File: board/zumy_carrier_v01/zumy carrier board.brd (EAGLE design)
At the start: 54 x 88.9 mm, 20 parts, among them J1 ODROID_POWER, J2 BATT_POWER, M1 POLOLU_STEP_DOWN, M2 ITG/MPU_MODULE, M3 POLOLU_DRV8833_MODULE, SW1 500SSP1S1M6QEA

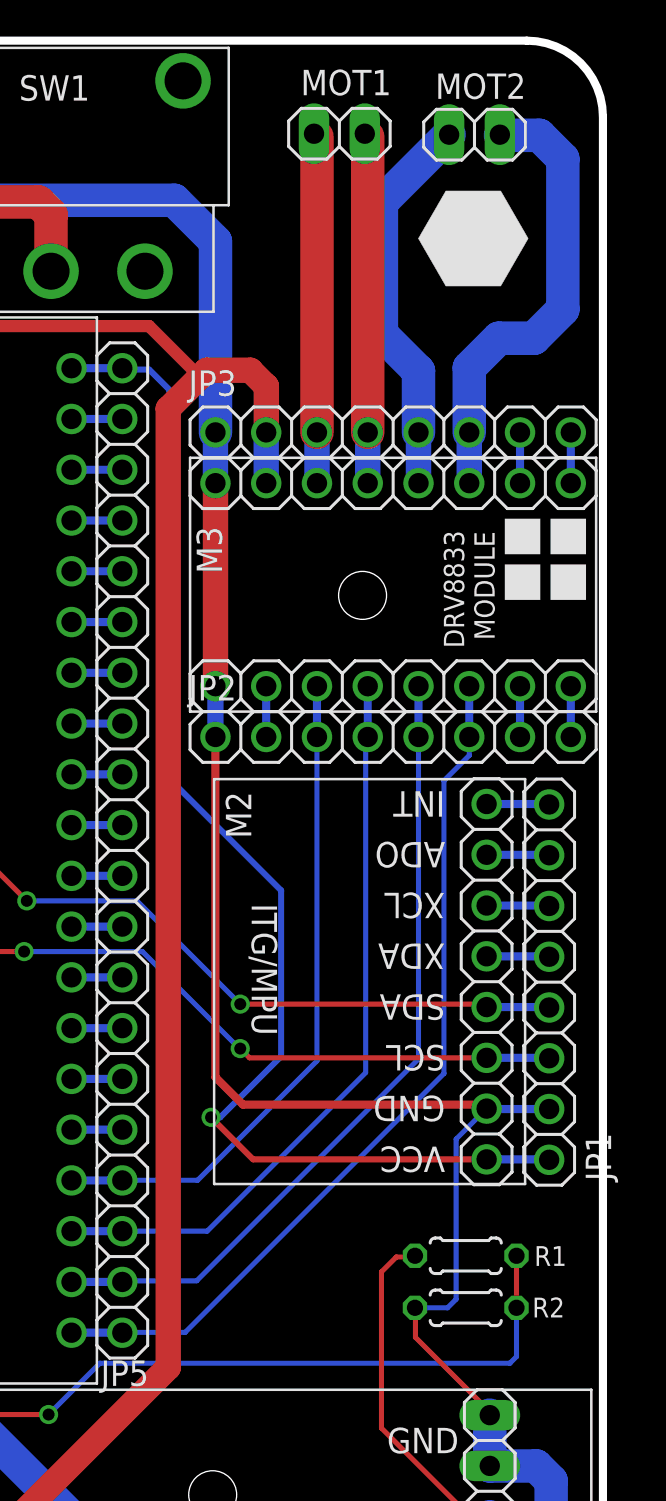
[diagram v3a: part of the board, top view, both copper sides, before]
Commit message: Added 6pin shrouded connectors for pololu encoder + motor drive. Routing is all screwed up.
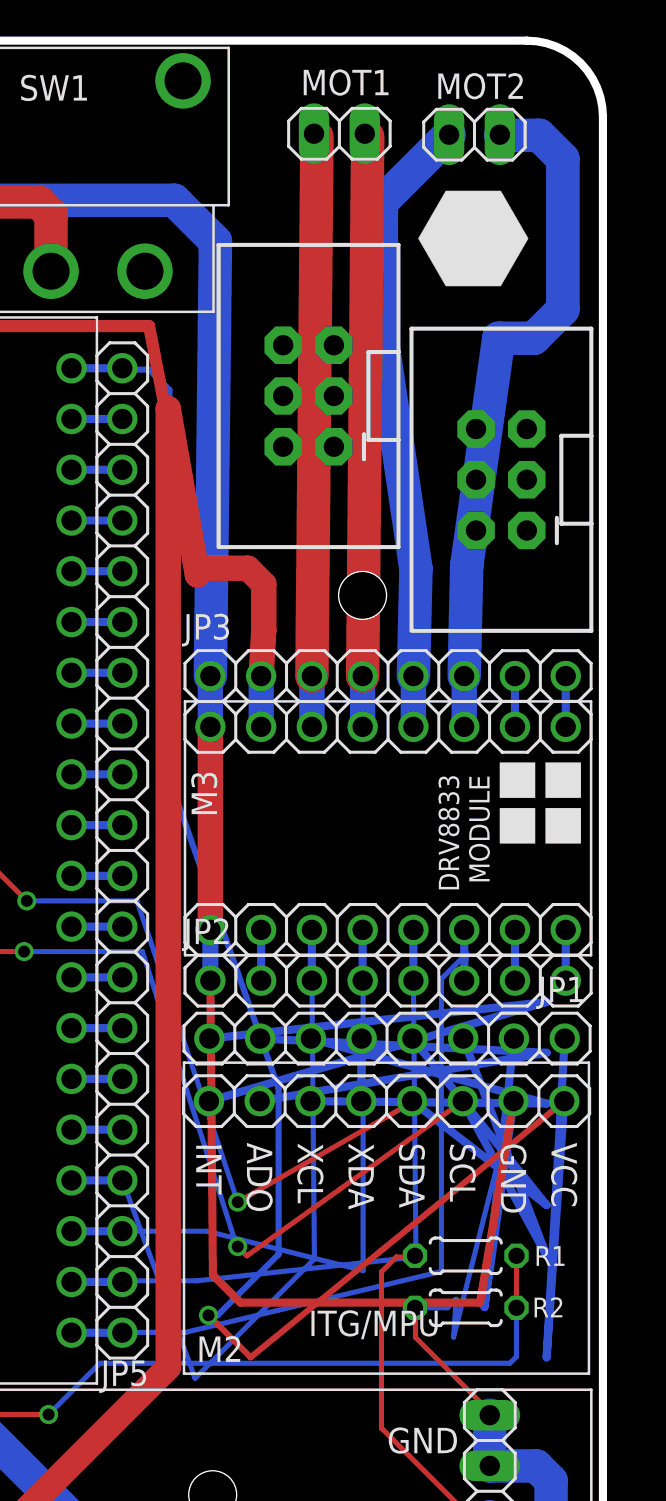
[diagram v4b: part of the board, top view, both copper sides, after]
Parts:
- added JP6, JP7: (no value), SparkFun-Connectors:2X3-SHROUDED
- moved M2 13.4 mm to (43.2, 28.6), turned to 0 degrees
- moved JP2 12.2 mm to (43.2, 41.9)
- moved M3 12.2 mm to (53.4, 43.1)
- moved JP3 12.2 mm to (43.2, 57.1)
- moved JP1 8.59 mm to (43.2, 39.0), turned to 0 degrees
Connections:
- removed net N$10: JP4.15, KIT1.P$15
- removed net N$24: JP4.16, KIT1.P$16
- removed net N$37: JP5.9, KIT1.P$29
- removed net N$38: JP5.10, KIT1.P$30
- removed net N$59: JP3.3, M3.BOUT1, MOT1.1
- removed net N$60: JP3.4, M3.BOUT2, MOT1.2
- removed net N$61: JP3.5, M3.AOUT2, MOT2.2
- removed net N$62: JP3.6, M3.AOUT1, MOT2.1
- new net MOTOR1_ENCA: JP5.10, JP6.1, KIT1.P$30
- new net MOTOR1_ENCB: JP5.9, JP6.3, KIT1.P$29
- new net MOTOR1_OUTA: JP3.6, JP6.2, M3.AOUT1, MOT2.1
- new net MOTOR1_OUTB: JP3.5, JP6.4, M3.AOUT2, MOT2.2
- new net MOTOR2_ENCA: JP4.15, JP7.1, KIT1.P$15
- new net MOTOR2_ENCB: JP4.16, JP7.3, KIT1.P$16
- new net MOTOR2_OUTA: JP3.3, JP7.2, M3.BOUT1, MOT1.1
- new net MOTOR2_OUTB: JP3.4, JP7.4, M3.BOUT2, MOT1.2
- net +3V3: now also JP6.5, JP7.5
- net GND: now also JP6.6, JP7.6
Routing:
- net GND: track 192.6 -> 237.2 mm
- net +3V3: track 63.6 -> 106.4 mm
- net MOTOR1_OUTA: track 0.00 -> 34.5 mm
- net N$1: track 3.15 -> 34.6 mm
- net MOTOR1_OUTB: track 0.00 -> 31.2 mm
- net MOTOR2_OUTB: track 0.00 -> 29.7 mm
- net MOTOR2_OUTA: track 0.00 -> 29.7 mm
- net MPU_SCL: track 54.3 -> 81.7 mm
- net N$2: track 3.15 -> 28.9 mm
- net N$62: track 22.9 -> 0.00 mm
- net MPU_SDA: track 54.3 -> 76.7 mm
- net N$3: track 3.15 -> 24.1 mm
- net N$61: track 19.6 -> 0.00 mm
- net +5V: track 131.7 -> 149.3 mm
- net N$60: track 17.5 -> 0.00 mm
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
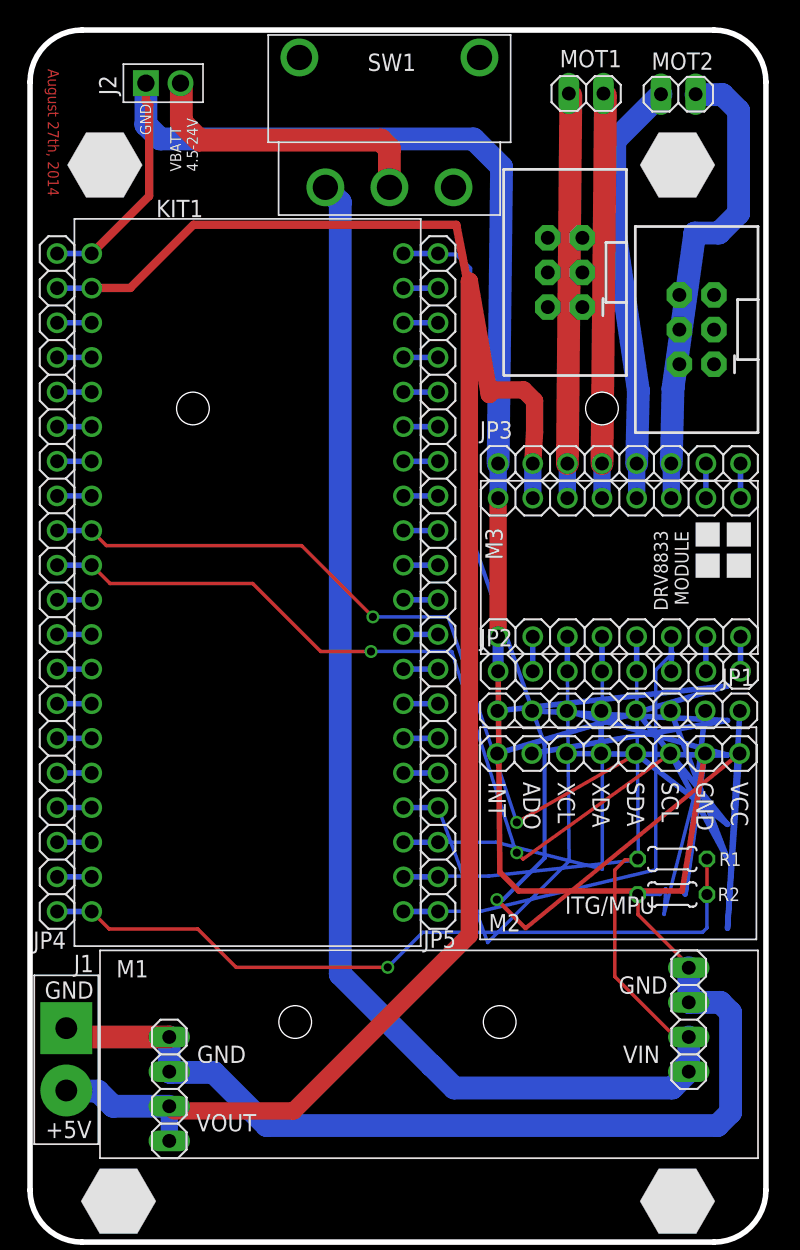
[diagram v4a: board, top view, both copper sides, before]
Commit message: Rev D now with encoder connectors, fully routed, no DRC errors.
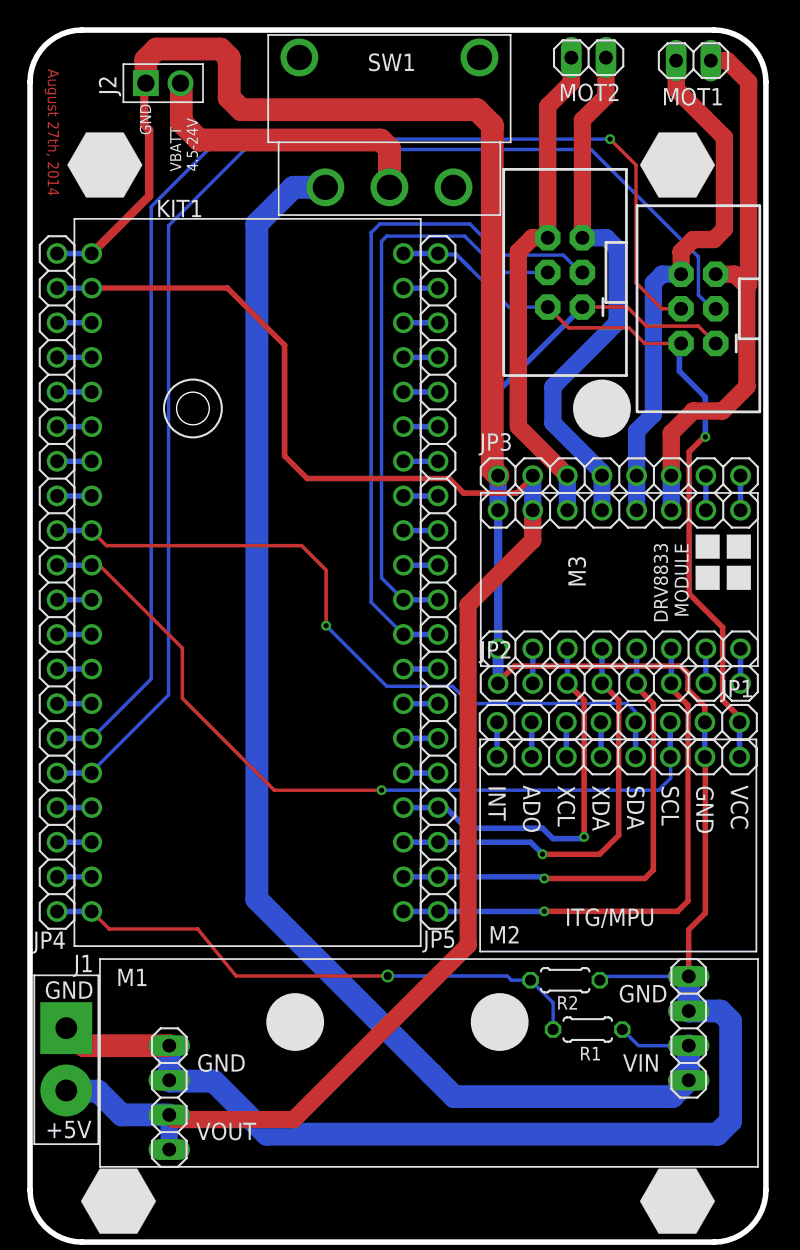
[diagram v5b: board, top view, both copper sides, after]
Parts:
- moved R1 14.0 mm to (40.9, 15.6), turned to 0 degrees
- moved R2 10.1 mm to (39.3, 19.2), turned to 180 degrees
- moved MOT1 8.24 mm to (48.7, 86.7)
- moved MOT2 7.10 mm to (41.0, 86.9), turned to 0 degrees
- moved JP7 1.53 mm to (49.0, 68.5)
- moved JP3 0.89 mm to (43.2, 56.2)
- moved M3 0.89 mm to (53.4, 42.2)
- moved M2 0.89 mm to (43.2, 27.7)
- moved JP2 0.89 mm to (43.2, 41.0)
- moved JP1 0.84 mm to (43.1, 38.1)
- moved M1 0.63 mm to (29.3, 13.1)
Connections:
- net +3V3: now also JP6.2, JP7.2; no longer JP6.5, JP7.5
- net GND: now also JP6.1, JP7.1; no longer JP6.6, JP7.6
- net MOTOR1_ENCA: now also JP6.4; no longer JP6.1
- net MOTOR1_OUTA: now also JP3.5, JP7.6, M3.AOUT2, MOT1.1; no longer JP3.6, JP6.2, M3.AOUT1, MOT2.1
- net MOTOR1_OUTB: now also JP3.6, JP7.5, M3.AOUT1, MOT1.2; no longer JP3.5, JP6.4, M3.AOUT2, MOT2.2
- net MOTOR2_ENCA: now also JP7.4; no longer JP7.1
- net MOTOR2_OUTA: now also JP6.6, MOT2.1; no longer JP7.2, MOT1.1
- net MOTOR2_OUTB: now also JP6.5, MOT2.2; no longer JP7.4, MOT1.2
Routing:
- net MOTOR2_ENCA: track 2.54 -> 94.5 mm, vias 0 -> 1
- net MOTOR2_ENCB: track 2.54 -> 93.9 mm
- net +3V3: track 106.4 -> 56.4 mm
- net MOTOR1_ENCB: track 2.54 -> 50.2 mm
- net MOTOR1_ENCA: track 2.54 -> 43.0 mm
- net N$1: track 34.6 -> 2.55 mm
- net +5V: track 149.3 -> 121.1 mm
- net N$2: track 28.9 -> 2.55 mm
- net MPU_SCL: track 81.7 -> 58.7 mm, vias 2 -> 1
- net MPU_SDA: track 76.7 -> 53.8 mm, vias 2 -> 1
- net N$3: track 24.1 -> 2.55 mm
- net V_BATT_SENSE: track 55.6 -> 41.3 mm
- net MOTOR1_OUTB: track 31.2 -> 41.1 mm
- net GND: track 237.2 -> 227.4 mm
- net MOTOR2_OUTB: track 29.7 -> 39.4 mm
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
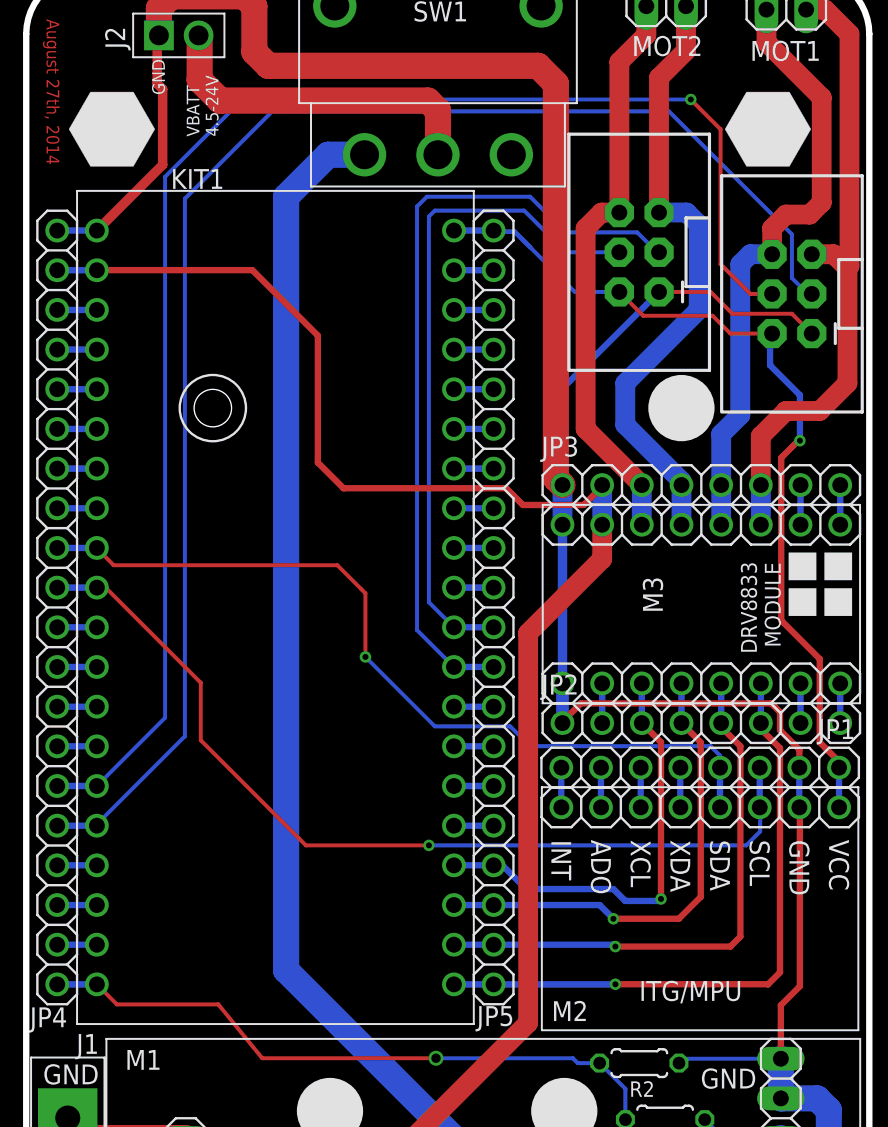
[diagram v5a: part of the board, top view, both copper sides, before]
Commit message: Rev D routed with schmitt triggers on encoders.
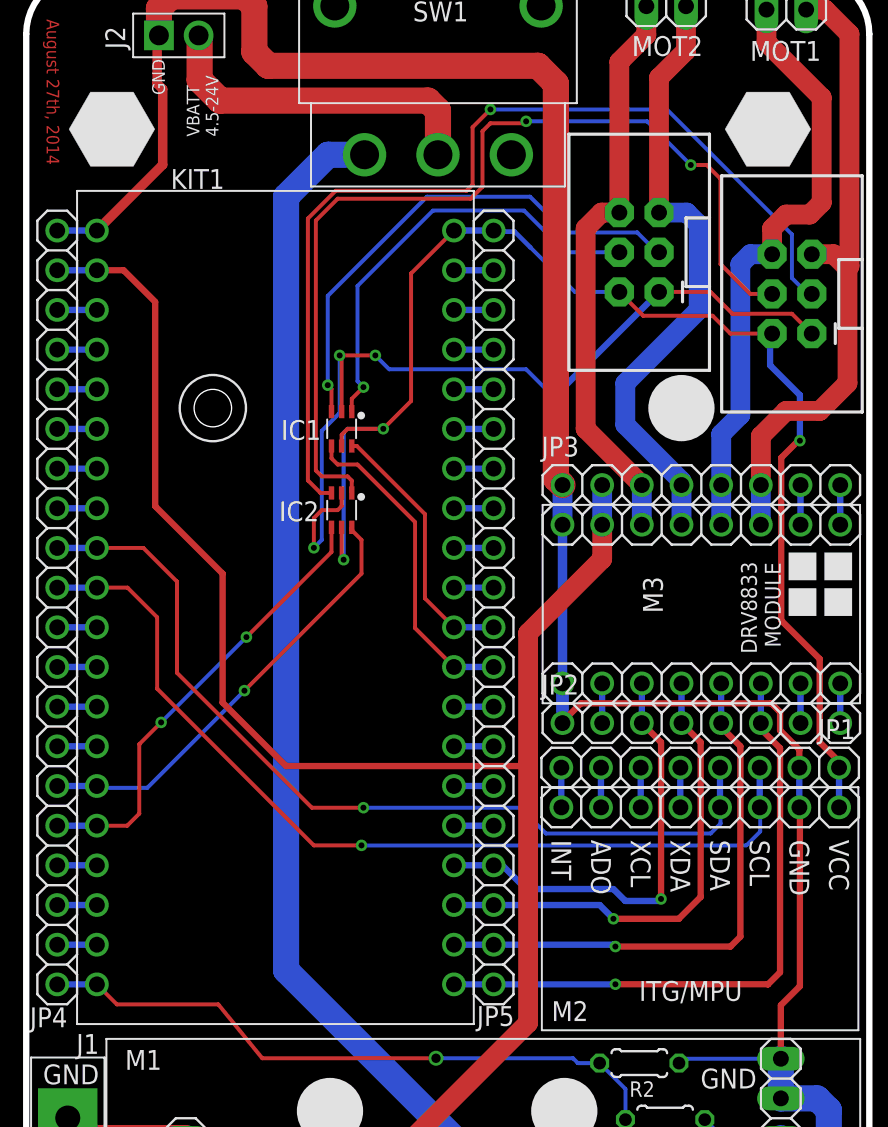
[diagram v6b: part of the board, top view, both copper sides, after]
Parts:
- added IC1, IC2: SN74AUP2G17, zumy:SC-70-6
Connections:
- new net M1_ENCA_DIG: IC1.6, JP5.10, KIT1.P$30
- new net M1_ENCB_DIG: IC1.4, JP5.9, KIT1.P$29
- new net M2_ENCA_DIG: IC2.6, JP4.15, KIT1.P$15
- new net M2_ENCB_DIG: IC2.4, JP4.16, KIT1.P$16
- net +3V3: now also IC1.5, IC2.5
- net GND: now also IC1.2, IC2.2
- net MOTOR1_ENCA: now also IC1.1; no longer JP5.10, KIT1.P$30
- net MOTOR1_ENCB: now also IC1.3; no longer JP5.9, KIT1.P$29
- net MOTOR2_ENCA: now also IC2.1; no longer JP4.15, KIT1.P$15
- net MOTOR2_ENCB: now also IC2.3; no longer JP4.16, KIT1.P$16
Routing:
- net GND: track 227.4 -> 263.8 mm, vias 0 -> 3
- net MOTOR2_ENCA: track 94.5 -> 61.1 mm, vias 1 -> 2
- net MOTOR2_ENCB: track 93.9 -> 62.4 mm, vias 0 -> 1
- net +3V3: track 56.4 -> 87.4 mm, vias 1 -> 3
- net M2_ENCB_DIG: track 0.00 -> 29.0 mm, vias 0 -> 2
- net M2_ENCA_DIG: track 0.00 -> 28.4 mm, vias 0 -> 1
- net M1_ENCB_DIG: track 0.00 -> 20.7 mm
- net MOTOR1_ENCB: track 50.2 -> 32.8 mm, vias 0 -> 1
- net M1_ENCA_DIG: track 0.00 -> 17.0 mm
- net MOTOR1_ENCA: track 43.0 -> 28.4 mm, vias 0 -> 1
- net +5V: track 121.1 -> 130.5 mm
- net MPU_SDA: track 53.8 -> 57.5 mm
- net MPU_SCL: track 58.7 -> 59.2 mm
